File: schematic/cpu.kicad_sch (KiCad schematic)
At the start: 1 part

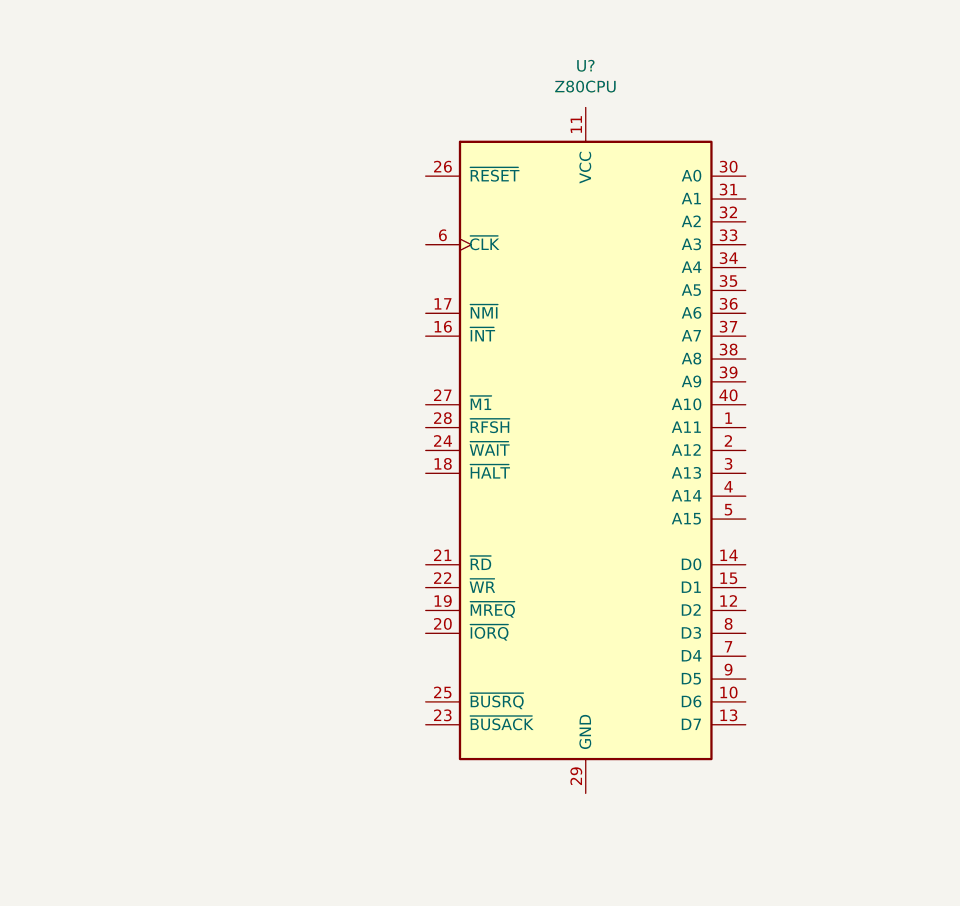
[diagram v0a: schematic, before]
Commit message: revised schematic into sheets for easier design. Looks much better.
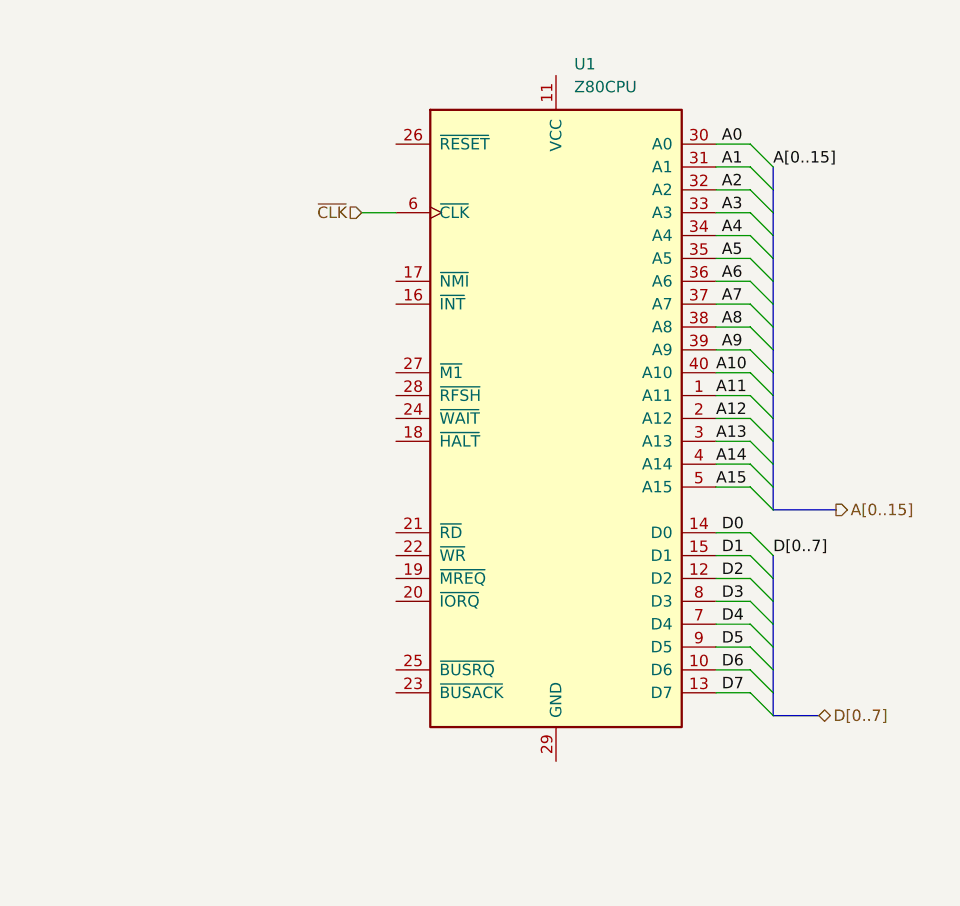
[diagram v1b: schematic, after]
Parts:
- removed U?: Z80CPU, symbol CPU:Z80CPU
- added U1: Z80CPU, symbol CPU:Z80CPU
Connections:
- new net A0: U1.30 (A0)
- new net A1: U1.31 (A1)
- new net A10: U1.40 (A10)
- new net A11: U1.1 (A11)
- new net A12: U1.2 (A12)
- new net A13: U1.3 (A13)
- new net A14: U1.4 (A14)
- new net A15: U1.5 (A15)
- new net A2: U1.32 (A2)
- new net A3: U1.33 (A3)
- new net A4: U1.34 (A4)
- new net A5: U1.35 (A5)
- new net A6: U1.36 (A6)
- new net A7: U1.37 (A7)
- new net A8: U1.38 (A8)
- new net A9: U1.39 (A9)
- new net D0: U1.14 (D0)
- new net D1: U1.15 (D1)
- new net D2: U1.12 (D2)
- new net D3: U1.8 (D3)
- new net D4: U1.7 (D4)
- new net D5: U1.9 (D5)
- new net D6: U1.10 (D6)
- new net D7: U1.13 (D7)
- new net ~{CLK}: U1.6 (~{CLK})

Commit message: Up to pin 29 on z80 done. Address 0 to 10 left. Only tracing to its end point for the most part. Each chip gets traced chip to chip in this manned
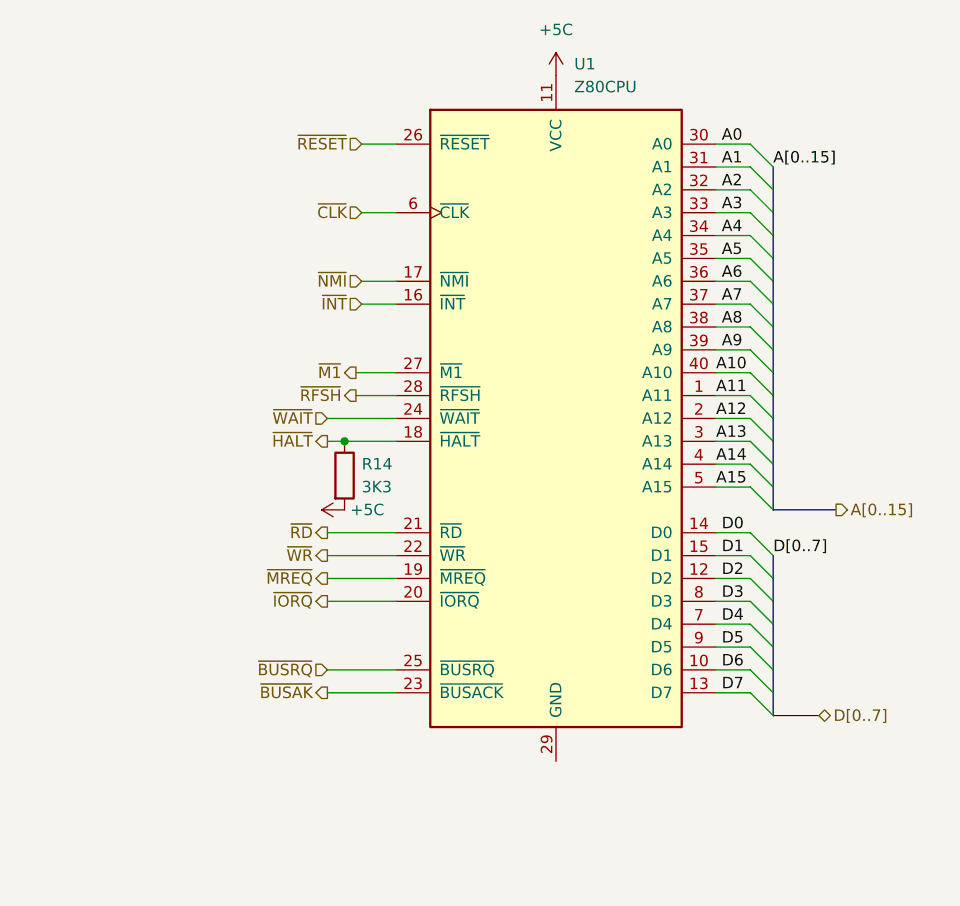
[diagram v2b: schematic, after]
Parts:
- added R14: 3K3, symbol Device:R
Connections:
- net +5C: now reaches U1.11 (VCC)
- net +5C: now also R14.2
- net ~{INT}: now reaches U1.16 (~{INT})
- net ~{NMI}: now reaches U1.17 (~{NMI})
- net ~{HALT}: now reaches U1.18 (~{HALT})
- net ~{HALT}: now also R14.1
- net ~{MREQ}: now reaches U1.19 (~{MREQ})
- net ~{IORQ}: now reaches U1.20 (~{IORQ})
- net ~{RD}: now reaches U1.21 (~{RD})
- net ~{WR}: now reaches U1.22 (~{WR})
- net ~{BUSAK}: now reaches U1.23 (~{BUSACK})
- net ~{WAIT}: now reaches U1.24 (~{WAIT})
- net ~{BUSRQ}: now reaches U1.25 (~{BUSRQ})
- net ~{RESET}: now reaches U1.26 (~{RESET})
- net ~{M1}: now reaches U1.27 (~{M1})
- net ~{RFSH}: now reaches U1.28 (~{RFSH})
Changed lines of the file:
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@@
 (kicad_sch (version 20211123) (generator eeschema)
   (paper "A4")
+  (junction (at 121.92 88.9) (diameter 0) (color 0 0 0 0)
+  )
   (bus_entry (at 167.005 78.74) (size 2.54 2.54)
     (stroke (width 0) (type default) (color 0 0 0 0))
@@
     (stroke (width 0) (type default) (color 0 0 0 0))
   )
+  (wire (pts (xy 120.015 104.14) (xy 127.635 104.14))
+    (stroke (width 0) (type default) (color 0 0 0 0))
+  )
   (bus (pts (xy 169.545 58.42) (xy 169.545 60.96))
     (stroke (width 0) (type default) (color 0 0 0 0))
@@
     (stroke (width 0) (type default) (color 0 0 0 0))
   )
+  (wire (pts (xy 123.825 71.12) (xy 127.635 71.12))
+    (stroke (width 0) (type default) (color 0 0 0 0))
+  )
   (wire (pts (xy 163.195 106.68) (xy 167.005 106.68))
     (stroke (width 0) (type default) (color 0 0 0 0))
   )
+  (wire (pts (xy 120.015 116.84) (xy 127.635 116.84))
+    (stroke (width 0) (type default) (color 0 0 0 0))
+  )
   (wire (pts (xy 163.195 58.42) (xy 167.005 58.42))
     (stroke (width 0) (type default) (color 0 0 0 0))
@@
     (stroke (width 0) (type default) (color 0 0 0 0))
   )
+  (wire (pts (xy 121.92 88.9) (xy 127.635 88.9))
+    (stroke (width 0) (type default) (color 0 0 0 0))
+  )
+  (wire (pts (xy 120.015 101.6) (xy 127.635 101.6))
+    (stroke (width 0) (type default) (color 0 0 0 0))
+  )
+  (wire (pts (xy 123.825 73.66) (xy 127.635 73.66))
+    (stroke (width 0) (type default) (color 0 0 0 0))
+  )
   (wire (pts (xy 163.195 91.44) (xy 167.005 91.44))
     (stroke (width 0) (type default) (color 0 0 0 0))
@@
     (stroke (width 0) (type default) (color 0 0 0 0))
   )
+  (wire (pts (xy 120.015 114.3) (xy 127.635 114.3))
+    (stroke (width 0) (type default) (color 0 0 0 0))
+  )
   (wire (pts (xy 163.195 83.82) (xy 167.005 83.82))
     (stroke (width 0) (type default) (color 0 0 0 0))
@@
     (stroke (width 0) (type default) (color 0 0 0 0))
   )
+  (wire (pts (xy 120.015 99.06) (xy 127.635 99.06))
+    (stroke (width 0) (type default) (color 0 0 0 0))
+  )
   (wire (pts (xy 163.195 111.76) (xy 167.005 111.76))
     (stroke (width 0) (type default) (color 0 0 0 0))
@@
     (stroke (width 0) (type default) (color 0 0 0 0))
   )
+  (wire (pts (xy 123.19 83.82) (xy 127.635 83.82))
+    (stroke (width 0) (type default) (color 0 0 0 0))
+  )
   (bus (pts (xy 169.545 111.76) (xy 169.545 114.3))
     (stroke (width 0) (type default) (color 0 0 0 0))
@@
     (stroke (width 0) (type default) (color 0 0 0 0))
   )
+  (wire (pts (xy 123.19 81.28) (xy 127.635 81.28))
+    (stroke (width 0) (type default) (color 0 0 0 0))
+  )
+  (wire (pts (xy 120.015 86.36) (xy 127.635 86.36))
+    (stroke (width 0) (type default) (color 0 0 0 0))
+  )
+  (wire (pts (xy 123.825 55.88) (xy 127.635 55.88))
+    (stroke (width 0) (type default) (color 0 0 0 0))
+  )
   (wire (pts (xy 163.195 101.6) (xy 167.005 101.6))
     (stroke (width 0) (type default) (color 0 0 0 0))
@@
     (stroke (width 0) (type default) (color 0 0 0 0))
   )
+  (wire (pts (xy 120.015 106.68) (xy 127.635 106.68))
+    (stroke (width 0) (type default) (color 0 0 0 0))
+  )
   (bus (pts (xy 169.545 73.66) (xy 169.545 76.2))
     (stroke (width 0) (type default) (color 0 0 0 0))
@@
     (stroke (width 0) (type default) (color 0 0 0 0))
   )
+  (wire (pts (xy 120.015 88.9) (xy 121.92 88.9))
+    (stroke (width 0) (type default) (color 0 0 0 0))
+  )
   (wire (pts (xy 163.195 73.66) (xy 167.005 73.66))
     (stroke (width 0) (type default) (color 0 0 0 0))
@@
   (label "A3" (at 163.83 63.5 0)
     (effects (font (size 1.27 1.27)) (justify left bottom))
+  )
+  (hierarchical_label "~{BUSRQ}" (shape input) (at 120.015 114.3 180)
+    (effects (font (size 1.27 1.27)) (justify right))
+  )
+  (hierarchical_label "~{RFSH}" (shape output) (at 123.19 83.82 180)
+    (effects (font (size 1.27 1.27)) (justify right))
   )
   (hierarchical_label "A[0..15]" (shape output) (at 176.53 96.52 0)
@@
     (effects (font (size 1.27 1.27)) (justify right))
   )
+  (hierarchical_label "~{WR}" (shape output) (at 120.015 101.6 180)
+    (effects (font (size 1.27 1.27)) (justify right))
+  )
+  (hierarchical_label "~{RD}" (shape output) (at 120.015 99.06 180)
+    (effects (font (size 1.27 1.27)) (justify right))
+  )
+  (hierarchical_label "~{RESET}" (shape input) (at 123.825 55.88 180)
+    (effects (font (size 1.27 1.27)) (justify right))
+  )
+  (hierarchical_label "~{INT}" (shape input) (at 123.825 73.66 180)
+    (effects (font (size 1.27 1.27)) (justify right))
+  )
+  (hierarchical_label "~{M1}" (shape output) (at 123.19 81.28 180)
+    (effects (font (size 1.27 1.27)) (justify right))
+  )
+  (hierarchical_label "~{MREQ}" (shape output) (at 120.015 104.14 180)
+    (effects (font (size 1.27 1.27)) (justify right))
+  )
+  (hierarchical_label "~{BUSAK}" (shape output) (at 120.015 116.84 180)
+    (effects (font (size 1.27 1.27)) (justify right))
+  )
   (hierarchical_label "D[0..7]" (shape bidirectional) (at 174.625 119.38 0)
     (effects (font (size 1.27 1.27)) (justify left))
+  )
+  (hierarchical_label "~{HALT}" (shape output) (at 120.015 88.9 180)
+    (effects (font (size 1.27 1.27)) (justify right))
+  )
+  (hierarchical_label "~{WAIT}" (shape input) (at 120.015 86.36 180)
+    (effects (font (size 1.27 1.27)) (justify right))
+  )
+  (hierarchical_label "~{NMI}" (shape input) (at 123.825 71.12 180)
+    (effects (font (size 1.27 1.27)) (justify right))
+  )
+  (hierarchical_label "~{IORQ}" (shape output) (at 120.015 106.68 180)
+    (effects (font (size 1.27 1.27)) (justify right))
   )
   (symbol (lib_id "CPU:Z80CPU") (at 145.415 86.36 0) (unit 1)
@@
     (pin "9")
   )
+  (symbol (lib_id "power:+5C") (at 145.415 48.26 0) (unit 1)
+    (in_bom yes) (on_board yes) (fields_autoplaced)
+    (property "Reference" "#PWR?" (id 0) (at 145.415 52.07 0)
+      (effects (font (size 1.27 1.27)) hide)
+    )
+    (property "Value" "+5C" (id 1) (at 145.415 43.18 0))
+    (property "Footprint" "" (id 2) (at 145.415 48.26 0)
+      (effects (font (size 1.27 1.27)) hide)
+    )
+    (property "Datasheet" "" (id 3) (at 145.415 48.26 0)
+      (effects (font (size 1.27 1.27)) hide)
+    )
+    (pin "1")
+  )
+  (symbol (lib_id "power:+5C") (at 121.92 96.52 90) (unit 1)
+    (in_bom yes) (on_board yes) (fields_autoplaced)
+    (property "Reference" "#PWR?" (id 0) (at 125.73 96.52 0)
+      (effects (font (size 1.27 1.27)) hide)
+    )
+    (property "Value" "+5C" (id 1) (at 122.555 96.5199 90)
+      (effects (font (size 1.27 1.27)) (justify right))
+    )
+    (property "Footprint" "" (id 2) (at 121.92 96.52 0)
+      (effects (font (size 1.27 1.27)) hide)
+    )
+    (property "Datasheet" "" (id 3) (at 121.92 96.52 0)
+      (effects (font (size 1.27 1.27)) hide)
+    )
+    (pin "1")
+  )
+  (symbol (lib_id "Device:R") (at 121.92 92.71 0) (unit 1)
+    (in_bom yes) (on_board yes) (fields_autoplaced)
+    (property "Reference" "R14" (id 0) (at 123.825 91.4399 0)
+      (effects (font (size 1.27 1.27)) (justify left))
+    )
+    (property "Value" "3K3" (id 1) (at 123.825 93.9799 0)
+      (effects (font (size 1.27 1.27)) (justify left))
+    )
+    (property "Footprint" "" (id 2) (at 120.142 92.71 90)
+      (effects (font (size 1.27 1.27)) hide)
+    )
+    (property "Datasheet" "~" (id 3) (at 121.92 92.71 0)
+      (effects (font (size 1.27 1.27)) hide)
+    )
+    (pin "1")
+    (pin "2")
+  )
 )

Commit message: added rf modulation schematic, added dram to vdp. Fixed +5vc to +5v
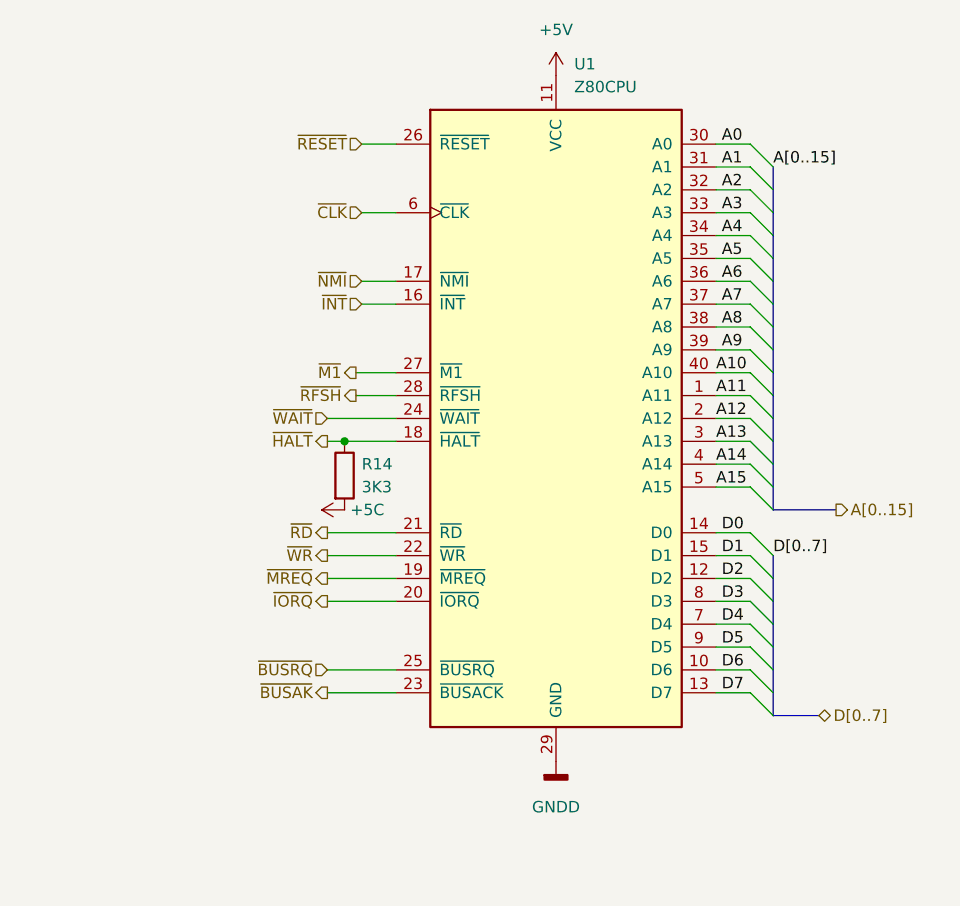
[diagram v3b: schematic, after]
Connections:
- net +5C: no longer U1.11 (VCC)
- net GNDD: now reaches U1.29 (GND)
- new net +5V: U1.11 (VCC)
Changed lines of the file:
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@@
     (effects (font (size 1.27 1.27)) (justify right))
+  )
+  (symbol (lib_id "power:+5V") (at 145.415 48.26 0) (unit 1)
+    (in_bom yes) (on_board yes) (fields_autoplaced)
+    (property "Reference" "#PWR?" (id 0) (at 145.415 52.07 0)
+      (effects (font (size 1.27 1.27)) hide)
+    )
+    (property "Value" "+5V" (id 1) (at 145.415 43.18 0))
+    (property "Footprint" "" (id 2) (at 145.415 48.26 0)
+      (effects (font (size 1.27 1.27)) hide)
+    )
+    (property "Datasheet" "" (id 3) (at 145.415 48.26 0)
+      (effects (font (size 1.27 1.27)) hide)
+    )
+    (pin "1")
   )
   (symbol (lib_id "CPU:Z80CPU") (at 145.415 86.36 0) (unit 1)
@@
     (pin "9")
   )
-  (symbol (lib_id "power:+5C") (at 145.415 48.26 0) (unit 1)
-    (in_bom yes) (on_board yes) (fields_autoplaced)
-    (property "Reference" "#PWR?" (id 0) (at 145.415 52.07 0)
-      (effects (font (size 1.27 1.27)) hide)
-    )
-    (property "Value" "+5C" (id 1) (at 145.415 43.18 0))
-    (property "Footprint" "" (id 2) (at 145.415 48.26 0)
-      (effects (font (size 1.27 1.27)) hide)
-    )
-    (property "Datasheet" "" (id 3) (at 145.415 48.26 0)
-      (effects (font (size 1.27 1.27)) hide)
-    )
-    (pin "1")
-  )
   (symbol (lib_id "power:+5C") (at 121.92 96.52 90) (unit 1)
     (in_bom yes) (on_board yes) (fields_autoplaced)
@@
       (effects (font (size 1.27 1.27)) hide)
     )
+    (pin "1")
+  )
+  (symbol (lib_id "power:GNDD") (at 145.415 124.46 0) (unit 1)
+    (in_bom yes) (on_board yes) (fields_autoplaced)
+    (property "Reference" "#PWR?" (id 0) (at 145.415 130.81 0)
+      (effects (font (size 1.27 1.27)) hide)
+    )
+    (property "Value" "GNDD" (id 1) (at 145.415 129.54 0))
+    (property "Footprint" "" (id 2) (at 145.415 124.46 0)
+      (effects (font (size 1.27 1.27)) hide)
+    )
+    (property "Datasheet" "" (id 3) (at 145.415 124.46 0)
+      (effects (font (size 1.27 1.27)) hide)
+    )
